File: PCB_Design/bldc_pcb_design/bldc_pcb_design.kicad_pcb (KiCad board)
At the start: 4 copper layers, 55.5 x 55.5 mm, 83 parts, among them IC1 DRV8305NPHPR, J1 Conn_01x06_Female, SW1 BOOT, SW2 RESET, T1 BC847, T2 BC847, U1 ESP32-WROOM-32D, U10 DS18S20Z+, U2 AS5600-ASOT, U3 LM2672M-3.3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

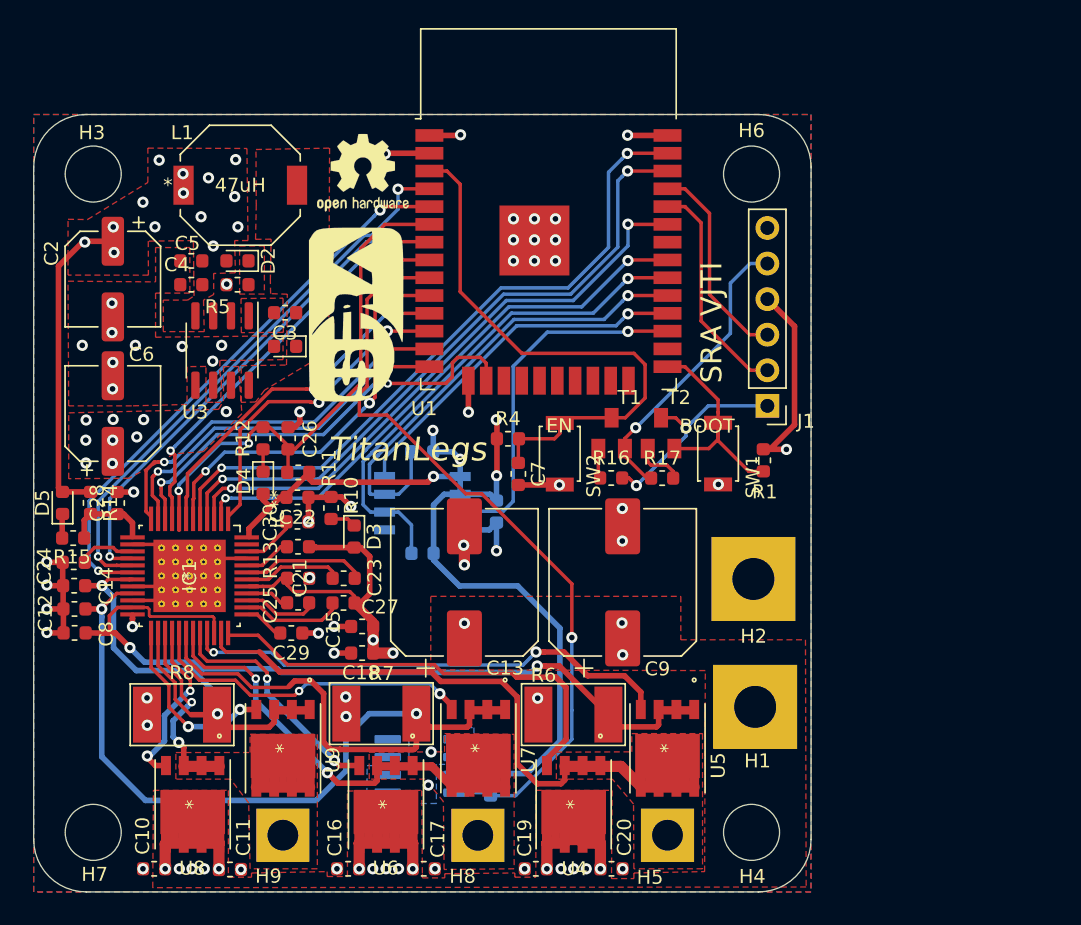
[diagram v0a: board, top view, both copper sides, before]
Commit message: Modified SilkScreen
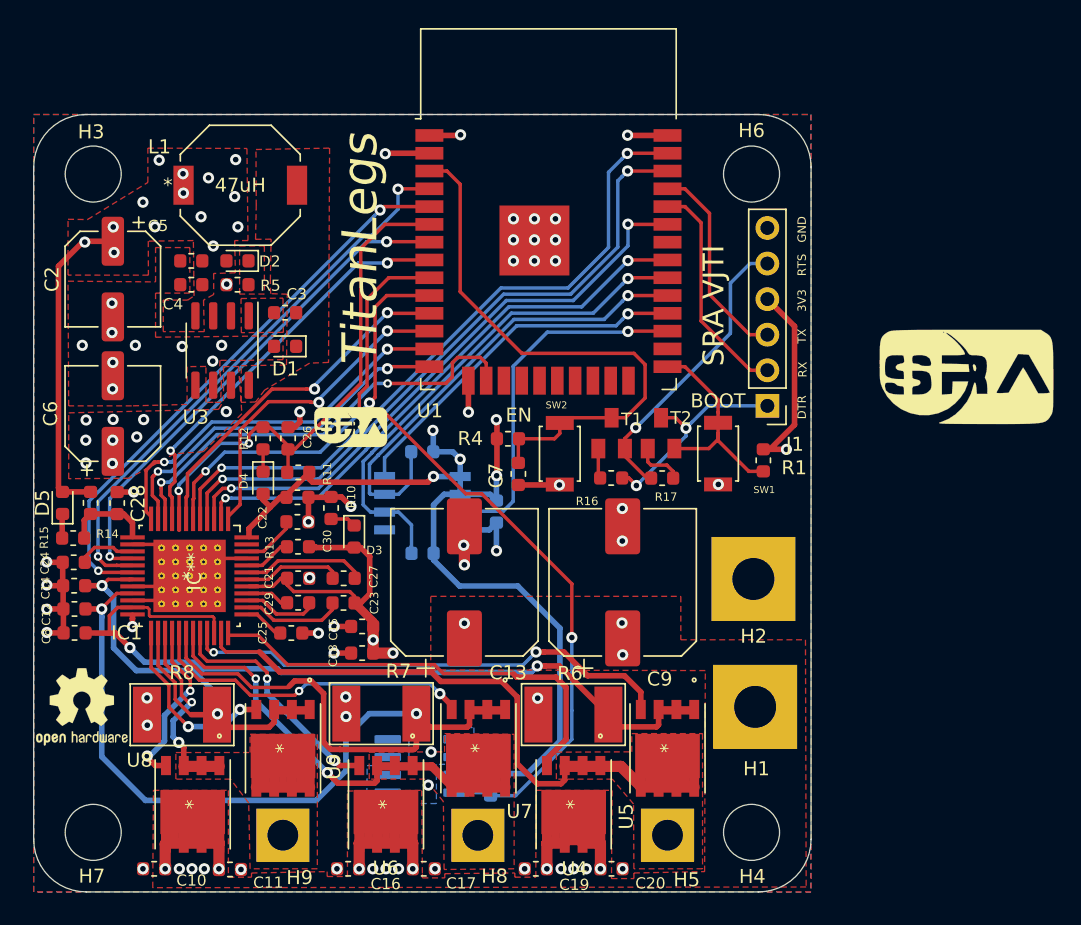
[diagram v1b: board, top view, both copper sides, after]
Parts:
- added G1: LOGO, Logos:sra_small, F.Cu at (88.4, 84.1)
- moved G*** 43.8 mm to (132.3, 80.5), turned to 0 degrees
- moved REF** 43.1 mm to (69.2, 104.0)
- moved G*** 3.12 mm to (93.4, 69.7)
- moved REF** 2.72 mm to (103.5, 97.5)
- moved G*** 2.63 mm to (78.7, 98.1)
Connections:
- net ~DTR renamed ~{DTR}
- net ~RTS renamed ~{RTS}
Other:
- net class Default removed
- board text added: "3V3"
- board text added: "DTR"
- board text added: "GND"
- board text added: "RTS"
- board text added: "RX"
- board text added: "TX"

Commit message: Update README.md
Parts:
- removed G1: LOGO, Logos:sra_small
- added G***: LOGO, Logos:sra_logo_smaller_neg, F.Cu at (68.7, 102.5)
- H3, H4, H6, H7: footprint MountingHole:MountingHole_4mm -> MountingHole:MountingHole_3.2mm_M3
- moved G*** 43.7 mm to (89.0, 74.9), turned to 90 degrees
- moved REF** 3.74 mm to (69.3, 107.8), turned to 90 degrees
- moved H3 1.04 mm to (69.3, 65.3)
- moved H6 1.00 mm to (117.7, 65.3)
- moved H7 0.98 mm to (69.3, 113.7)
- moved H4 0.94 mm to (117.7, 113.7)
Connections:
- IC1 pad 47: Net-(IC1-Pad47) -> unconnected-(IC1-Pad47)
- IC1 pad 49: GND -> (no net)
- IC1 pad V: GND -> (no net)
- U1 pad 17: Net-(U1-Pad17) -> unconnected-(U1-Pad17)
- U1 pad 18: Net-(U1-Pad18) -> unconnected-(U1-Pad18)
- U1 pad 19: Net-(U1-Pad19) -> unconnected-(U1-Pad19)
- U1 pad 20: Net-(U1-Pad20) -> unconnected-(U1-Pad20)
- U1 pad 21: Net-(U1-Pad21) -> unconnected-(U1-Pad21)
- U1 pad 22: Net-(U1-Pad22) -> unconnected-(U1-Pad22)
- U1 pad 23: Net-(U1-Pad23) -> unconnected-(U1-Pad23)
- U1 pad 24: Net-(U1-Pad24) -> unconnected-(U1-Pad24)
- U1 pad 26: Net-(U1-Pad26) -> unconnected-(U1-Pad26)
- U1 pad 32: Net-(U1-Pad32) -> unconnected-(U1-Pad32)
- U10 pad 1: GND -> (no net)
- U10 pad 2: GND -> (no net)
- U10 pad 6: GND -> (no net)
- U2 pad 5: Net-(U2-Pad5) -> unconnected-(U2-Pad5)
- U3 pad 2: Net-(U3-Pad2) -> unconnected-(U3-Pad2)
- U3 pad 3: Net-(U3-Pad3) -> unconnected-(U3-Pad3)
- U3 pad 5: Net-(U3-Pad5) -> unconnected-(U3-Pad5)
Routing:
- net GLA: track 35.4 -> 28.3 mm, vias 2 -> 1
- net POWER_IN: track 45.0 -> 46.3 mm
- net TEMP_DQ: track 54.8 -> 55.9 mm
- net DRV_nFAULT: track 38.1 -> 37.2 mm
- net SLA: track 58.4 -> 57.4 mm, vias 2 -> 3
- net DRV_EN_GATE: track 23.1 -> 24.0 mm
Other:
- board text added: "PWRIN"
